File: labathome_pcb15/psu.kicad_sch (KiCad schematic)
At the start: 38 parts, among them J8 POWER, J9 Barrel_Jack_Switch, SW11 PROG 5V POWER, SW5 POWER, U11 AMS1117, U2 IP5306, U24 SRV05, U27 TPS54202DDC

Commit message: labathome15 v0.0.1
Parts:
- added DRAWING1: Polarity, liebler_DRAWINGS:barrel_jack_positive_polarity, symbol Mechanical:Fiducial
- added SW4: BATT POWER, liebler_MECH:Switch_SS12D00, symbol Switch:SW_SPDT
- L1: footprint Inductor_SMD:L_Abracon_ASPI-0630LR -> liebler_PASSIVES:L_0630
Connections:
- net +5V: now also SW4.1 (A); no longer C28.2, C30.2, C31.2, U2.8 (VOUT)
- new net: C28.2, C30.2, C31.2, SW4.2 (B), U2.8 (VOUT)
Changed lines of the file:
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@@
 	)
 	(junction
-		(at 219.71 33.02)
-		(diameter 0)
-		(color 0 0 0 0)
-	)
-	(junction
 		(at 166.37 38.1)
 		(diameter 0)
@@
 	)
 	(junction
+		(at 219.71 33.02)
+		(diameter 0)
+		(color 0 0 0 0)
+	)
+	(junction
 		(at 218.44 35.56)
 		(diameter 0)
@@
 	(wire
 		(pts
+			(xy 246.38 31.75) (xy 226.06 31.75)
+		)
+		(stroke
+			(width 0)
+			(type default)
+		)
+	)
+	(wire
+		(pts
 			(xy 208.28 50.8) (xy 218.44 50.8)
 		)
@@
 	(wire
 		(pts
+			(xy 226.06 31.75) (xy 226.06 33.02)
+		)
+		(stroke
+			(width 0)
+			(type default)
+		)
+	)
+	(wire
+		(pts
 			(xy 80.01 20.32) (xy 80.01 25.4)
 		)
@@
 	(wire
 		(pts
+			(xy 226.06 33.02) (xy 219.71 33.02)
+		)
+		(stroke
+			(width 0)
+			(type default)
+		)
+	)
+	(wire
+		(pts
 			(xy 186.69 33.02) (xy 199.39 33.02)
 		)
@@
 	)
 	(symbol
+		(lib_id "Switch:SW_SPDT")
+		(at 251.46 31.75 0)
+		(unit 1)
+		(exclude_from_sim no)
+		(in_bom yes)
+		(on_board yes)
+		(dnp no)
+		(property "Reference" "SW4"
+			(at 251.46 24.511 0)
+			(effects
+				(font
+					(size 1.27 1.27)
+				)
+			)
+		)
+		(property "Value" "BATT POWER"
+			(at 251.46 36.576 0)
+			(effects
+				(font
+					(size 1.27 1.27)
+				)
+			)
+		)
+		(property "Footprint" "liebler_MECH:Switch_SS12D00"
+			(at 251.46 31.75 0)
+			(effects
+				(font
+					(size 1.27 1.27)
+				)
+				(hide yes)
+			)
+		)
+		(property "Datasheet" "~"
+			(at 251.46 31.75 0)
+			(effects
+				(font
+					(size 1.27 1.27)
+				)
+				(hide yes)
+			)
+		)
+		(property "Description" ""
+			(at 251.46 31.75 0)
+			(effects
+				(font
+					(size 1.27 1.27)
+				)
+				(hide yes)
+			)
+		)
+		(pin "1"
+		)
+		(pin "2"
+		)
+		(pin "3"
+		)
+		(instances
+			(project "labathome_pcb15"
+				(path "/e4d6926a-1a8b-424d-97c4-66b6ad87e4ac/77dfbe0c-d674-478a-bf0e-cfa040fb2e8f"
+					(reference "SW4")
+					(unit 1)
+				)
+			)
+		)
+	)
+	(symbol
 		(lib_id "power:GND")
 		(at 199.39 25.4 180)
@@
 			)
 		)
-		(property "Footprint" "Inductor_SMD:L_Abracon_ASPI-0630LR"
+		(property "Footprint" "liebler_PASSIVES:L_0630"
 			(at 190.5 35.56 0)
 			(effects
@@
 	(symbol
 		(lib_id "power:+5V")
-		(at 219.71 33.02 270)
+		(at 256.54 29.21 270)
+		(mirror x)
 		(unit 1)
 		(exclude_from_sim no)
@@
 		(on_board yes)
 		(dnp no)
-		(fields_autoplaced yes)
 		(property "Reference" "#PWR035"
-			(at 215.9 33.02 0)
+			(at 252.73 29.21 0)
 			(effects
 				(font
@@
 		)
 		(property "Value" "+5V"
-			(at 223.52 33.0199 90)
+			(at 260.35 29.2101 90)
 			(effects
 				(font
@@
 		)
 		(property "Footprint" ""
-			(at 219.71 33.02 0)
+			(at 256.54 29.21 0)
 			(effects
 				(font
@@
 		)
 		(property "Datasheet" ""
-			(at 219.71 33.02 0)
+			(at 256.54 29.21 0)
 			(effects
 				(font
@@
 		)
 		(property "Description" ""
-			(at 219.71 33.02 0)
+			(at 256.54 29.21 0)
 			(effects
 				(font
@@
 					(unit 1)
 				)
+			)
+		)
+	)
+	(symbol
+		(lib_id "Mechanical:Fiducial")
+		(at 97.79 72.39 0)
+		(unit 1)
+		(exclude_from_sim yes)
+		(in_bom no)
+		(on_board yes)
+		(dnp no)
+		(fields_autoplaced yes)
+		(property "Reference" "DRAWING1"
+			(at 100.33 71.1199 0)
+			(effects
+				(font
+					(size 1.27 1.27)
+				)
+				(justify left)
+			)
+		)
+		(property "Value" "Polarity"
+			(at 100.33 73.6599 0)
+			(effects
+				(font
+					(size 1.27 1.27)
+				)
+				(justify left)
+			)
+		)
+		(property "Footprint" "liebler_DRAWINGS:barrel_jack_positive_polarity"
+			(at 97.79 72.39 0)
+			(effects
+				(font
+					(size 1.27 1.27)
+				)
+				(hide yes)
+			)
+		)
+		(property "Datasheet" "~"
+			(at 97.79 72.39 0)
+			(effects
+				(font
+					(size 1.27 1.27)
+				)
+				(hide yes)
+			)
+		)
+		(property "Description" "Fiducial Marker"
+			(at 97.79 72.39 0)
+			(effects
+				(font
+					(size 1.27 1.27)
+				)
+				(hide yes)
+			)
+		)
+		(instances
+			(project ""
+				(path "/e4d6926a-1a8b-424d-97c4-66b6ad87e4ac/77dfbe0c-d674-478a-bf0e-cfa040fb2e8f"
+					(reference "DRAWING1")
+					(unit 1)
+				)

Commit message: labathome_pcb15
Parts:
- added R47: 1R, Resistor_SMD:R_0603_1608Metric, symbol Device:R
- added R48: 3k3, Resistor_SMD:R_0402_1005Metric, symbol Device:R
- C41, C42, C43, C44: footprint Capacitor_SMD:C_0603_1608Metric -> Capacitor_SMD:C_0402_1005Metric
- C79: value u1 -> u1/35V
- C80: value 10u -> 10u/35V
- C81: value u1 -> u1/16V
- R3: value 2R2 -> 1R
- R4: footprint Resistor_SMD:R_0603_1608Metric -> Resistor_SMD:R_0402_1005Metric
- R60: value 13k3 -> 10k
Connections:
- net +5P: now also R47.1; no longer R3.1
- net GND: now also R48.1; no longer R60.1
- new net: R48.2, R60.1
- new net: R3.1, R47.2
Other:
- moved on the sheet: C1

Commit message: labathome_pcb5 ready for review, 2nd
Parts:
- removed DRAWING1: Polarity, liebler_DRAWINGS:barrel_jack_positive_polarity, symbol Mechanical:Fiducial
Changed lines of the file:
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@@
-	)
-	(symbol
-		(lib_id "Mechanical:Fiducial")
-		(at 97.79 72.39 0)
-		(unit 1)
-		(exclude_from_sim yes)
-		(in_bom no)
-		(on_board yes)
-		(dnp no)
-		(fields_autoplaced yes)
-		(property "Reference" "DRAWING1"
-			(at 100.33 71.1199 0)
-			(effects
-				(font
-					(size 1.27 1.27)
-				)
-				(justify left)
-			)
-		)
-		(property "Value" "Polarity"
-			(at 100.33 73.6599 0)
-			(effects
-				(font
-					(size 1.27 1.27)
-				)
-				(justify left)
-			)
-		)
-		(property "Footprint" "liebler_DRAWINGS:barrel_jack_positive_polarity"
-			(at 97.79 72.39 0)
-			(effects
-				(font
-					(size 1.27 1.27)
-				)
-				(hide yes)
-			)
-		)
-		(property "Datasheet" "~"
-			(at 97.79 72.39 0)
-			(effects
-				(font
-					(size 1.27 1.27)
-				)
-				(hide yes)
-			)
-		)
-		(property "Description" "Fiducial Marker"
-			(at 97.79 72.39 0)
-			(effects
-				(font
-					(size 1.27 1.27)
-				)
-				(hide yes)
-			)
-		)
-		(instances
-			(project ""
-				(path "/e4d6926a-1a8b-424d-97c4-66b6ad87e4ac/77dfbe0c-d674-478a-bf0e-cfa040fb2e8f"
-					(reference "DRAWING1")
-					(unit 1)
-				)
-			)
-		)
 	)
 	(symbol

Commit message: Further improventents in PCB layout
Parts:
- J8: symbol Connector:USB_C_Receptacle_USB2.0 -> Connector:USB_C_Receptacle_USB2.0_16P
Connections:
- no-connect marks 4 -> 5
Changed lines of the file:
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@@
 	)
 	(junction
+		(at 213.36 35.56)
+		(diameter 0)
+		(color 0 0 0 0)
+	)
+	(junction
 		(at 218.44 35.56)
 		(diameter 0)
@@
 		(at 40.64 52.07)
 	)
+	(no_connect
+		(at 256.54 34.29)
+	)
 	(wire
 		(pts
@@
 	(wire
 		(pts
-			(xy 208.28 35.56) (xy 218.44 35.56)
+			(xy 208.28 35.56) (xy 213.36 35.56)
 		)
 		(stroke
@@
 		)
 	)
+	(wire
+		(pts
+			(xy 213.36 35.56) (xy 218.44 35.56)
+		)
+		(stroke
+			(width 0)
+			(type default)
+		)
+	)
 	(polyline
 		(pts
@@
 			)
 		)
-		(property "Description" ""
+		(property "Description" "Power symbol creates a global label with name \"+5VP\""
 			(at 121.92 33.02 0)
 			(effects
@@
 			)
 		)
-		(property "Description" ""
+		(property "Description" "Power symbol creates a global label with name \"GND\" , ground"
 			(at 209.55 25.4 0)
 			(effects
@@
 			)
 		)
-		(property "Description" ""
+		(property "Description" "Power symbol creates a global label with name \"+5P\""
 			(at 100.33 100.33 0)
 			(effects
@@
 			)
 		)
-		(property "Description" ""
+		(property "Description" "Power symbol creates a global label with name \"+5V\""
 			(at 110.49 102.87 0)
 			(effects
@@
 			)
 		)
-		(property "Description" ""
+		(property "Description" "Power symbol creates a global label with name \"+24V\""
 			(at 82.55 80.01 0)
 			(effects
@@
 			)
 		)
-		(property "Description" ""
+		(property "Description" "Switch, single pole double throw"
 			(at 251.46 31.75 0)
 			(effects
@@
 			)
 		)
-		(property "Description" ""
+		(property "Description" "Power symbol creates a global label with name \"GND\" , ground"
 			(at 199.39 25.4 0)
 			(effects
@@
 			)
 		)
-		(property "Description" ""
+		(property "Description" "Power symbol creates a global label with name \"+5V\""
 			(at 17.78 73.66 0)
 			(effects
@@
 			)
 		)
-		(property "Description" ""
+		(property "Description" "Power symbol creates a global label with name \"+24V\""
 			(at 48.26 21.59 0)
 			(effects
@@
 			)
 		)
-		(property "Description" ""
+		(property "Description" "Power symbol creates a global label with name \"GND\" , ground"
 			(at 171.45 52.07 0)
 			(effects
@@
 			)
 		)
-		(property "Description" ""
+		(property "Description" "Power symbol creates a global label with name \"GND\" , ground"
 			(at 43.18 124.46 0)
 			(effects
@@
 			)
 		)
-		(property "Description" ""
+		(property "Description" "Special symbol for telling ERC where power comes from"
 			(at 110.49 102.87 0)
 			(effects
@@
 			)
 		)
-		(property "Description" ""
+		(property "Description" "1A Low Dropout regulator, positive, 3.3V fixed output, SOT-223"
 			(at 38.1 73.66 0)
 			(effects
@@
 			)
 		)
-		(property "Description" ""
+		(property "Description" "Power symbol creates a global label with name \"GND\" , ground"
 			(at 179.07 44.45 0)
 			(effects
@@
 			)
 		)
-		(property "Description" ""
+		(property "Description" "Power symbol creates a global label with name \"+5V\""
 			(at 256.54 29.21 0)
 			(effects
@@
 			)
 		)
-		(property "Description" ""
+		(property "Description" "Special symbol for telling ERC where power comes from"
 			(at 40.64 21.59 0)
 			(effects
@@
 			)
 		)
-		(property "Description" ""
+		(property "Description" "Special symbol for telling ERC where power comes from"
 			(at 91.44 105.41 0)
 			(effects
@@
 			)
 		)
-		(property "Description" ""
+		(property "Description" "Switch, single pole double throw"
 			(at 105.41 102.87 0)
 			(effects
@@
 			)
 		)
-		(property "Description" ""
+		(property "Description" "Power symbol creates a global label with name \"GND\" , ground"
 			(at 55.88 81.28 0)
 			(effects
@@
 			)
 		)
-		(property "Description" ""
+		(property "Description" "Power symbol creates a global label with name \"GND\" , ground"
 			(at 194.31 50.8 0)
 			(effects
@@
 			)
 		)
-		(property "Description" ""
+		(property "Description" "Power symbol creates a global label with name \"GND\" , ground"
 			(at 80.01 50.8 0)
 			(effects
@@
 	)
 	(symbol
-		(lib_id "Connector:USB_C_Receptacle_USB2.0")
+		(lib_id "Connector:USB_C_Receptacle_USB2.0_16P")
 		(at 25.4 36.83 0)
 		(unit 1)
@@
 			)
 		)
-		(property "Description" ""
+		(property "Description" "USB 2.0-only 16P Type-C Receptacle connector"
 			(at 25.4 36.83 0)
 			(effects
@@
 			)
 		)
-		(property "Description" ""
+		(property "Description" "Power symbol creates a global label with name \"GND\" , ground"
 			(at 219.71 25.4 0)
 			(effects
@@
 			)
 		)
-		(property "Description" ""
+		(property "Description" "Power symbol creates a global label with name \"GND\" , ground"
 			(at 132.08 57.15 0)
 			(effects
@@
 			)
 		)
-		(property "Description" ""
+		(property "Description" "Power symbol creates a global label with name \"GND\" , ground"
 			(at 82.55 74.93 0)
 			(effects
@@
 			)
 		)
-		(property "Description" ""
+		(property "Description" "Power symbol creates a global label with name \"+3V8\""
 			(at 218.44 35.56 0)
 			(effects
@@
 			)
 		)
-		(property "Description" ""
+		(property "Description" "Power symbol creates a global label with name \"GND\" , ground"
 			(at 25.4 59.69 0)
 			(effects
@@
 			)
 		)
-		(property "Description" ""
+		(property "Description" "Power symbol creates a global label with name \"+3V3\""
 			(at 55.88 73.66 0)
 			(effects
@@
 			)
 		)
-		(property "Description" ""
+		(property "Description" "Power symbol creates a global label with name \"+24V\""
 			(at 25.4 106.68 0)
 			(effects
@@
 	)
 	(symbol
+		(lib_id "power:PWR_FLAG")
+		(at 213.36 35.56 180)
+		(unit 1)
+		(exclude_from_sim no)
+		(in_bom yes)
+		(on_board yes)
+		(dnp no)
+		(fields_autoplaced yes)
+		(property "Reference" "#FLG09"
+			(at 213.36 37.465 0)
+			(effects
+				(font
+					(size 1.27 1.27)
+				)
+				(hide yes)
+			)
+		)
+		(property "Value" "PWR_FLAG"
+			(at 213.36 40.64 0)
+			(effects
+				(font
+					(size 1.27 1.27)
+				)
+			)
+		)
+		(property "Footprint" ""
+			(at 213.36 35.56 0)
+			(effects
+				(font
+					(size 1.27 1.27)
+				)
+				(hide yes)
+			)
+		)
+		(property "Datasheet" "~"
+			(at 213.36 35.56 0)
+			(effects
+				(font
+					(size 1.27 1.27)
+				)
+				(hide yes)
+			)
+		)
+		(property "Description" "Special symbol for telling ERC where power comes from"
+			(at 213.36 35.56 0)
+			(effects
+				(font
+					(size 1.27 1.27)
+				)
+				(hide yes)
+			)
+		)
+		(pin "1"
+		)
+		(instances
+			(project ""
+				(path "/e4d6926a-1a8b-424d-97c4-66b6ad87e4ac/77dfbe0c-d674-478a-bf0e-cfa040fb2e8f"
+					(reference "#FLG09")
+					(unit 1)
+				)
+			)
+		)
+	)
+	(symbol
 		(lib_id "Device:Battery_Cell")
 		(at 218.44 44.45 0)
@@
 			)
 		)
-		(property "Description" ""
+		(property "Description" "Single-cell battery"
 			(at 218.44 44.45 0)
 			(effects

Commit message: lbathome 15.1
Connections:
- net USBPD_CC1: now also U24.3 (IO2); no longer U24.1 (IO1)
- net USBPD_D-: now also U24.1 (IO1); no longer U24.3 (IO2)
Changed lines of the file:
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@@
 	(global_label "USBPD_D-"
 		(shape input)
-		(at 92.71 40.64 0)
+		(at 92.71 35.56 0)
 		(fields_autoplaced yes)
 		(effects
@@
 		)
 		(property "Intersheetrefs" "${INTERSHEET_REFS}"
-			(at 105.8552 40.64 0)
+			(at 105.8552 35.56 0)
 			(effects
 				(font
@@
 	(global_label "USBPD_CC1"
 		(shape input)
-		(at 92.71 35.56 0)
+		(at 92.71 40.64 0)
 		(fields_autoplaced yes)
 		(effects
@@
 		)
 		(property "Intersheetrefs" "${INTERSHEET_REFS}"
-			(at 106.7623 35.56 0)
+			(at 106.7623 40.64 0)
 			(effects
 				(font

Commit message: Updates in PCB, arduino test firmware
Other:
- company: (none) -> Klaus Liebler
- title: (none) -> lab@home
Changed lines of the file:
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@@
 	(generator_version "8.0")
 	(paper "A4")
+	(title_block
+		(title "lab@home")
+		(date "2024-08-19")
+		(rev "15.1")
+		(company "Klaus Liebler")
+	)
 	(junction
 		(at 157.48 45.72)

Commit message: Various last minute
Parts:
- C81: footprint Capacitor_SMD:C_0402_1005Metric -> Capacitor_SMD:C_0603_1608Metric
- R4, R48, R59, R60: footprint Resistor_SMD:R_0402_1005Metric -> Resistor_SMD:R_0201_0603Metric
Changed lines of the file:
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@@
 			)
 		)
-		(property "Footprint" "Resistor_SMD:R_0402_1005Metric"
+		(property "Footprint" "Resistor_SMD:R_0201_0603Metric"
 			(at 88.138 124.46 90)
 			(effects
@@
 			)
 		)
-		(property "Footprint" "Resistor_SMD:R_0402_1005Metric"
+		(property "Footprint" "Resistor_SMD:R_0201_0603Metric"
 			(at 88.138 116.84 90)
 			(effects
@@
 			)
 		)
-		(property "Footprint" "Resistor_SMD:R_0402_1005Metric"
+		(property "Footprint" "Resistor_SMD:R_0201_0603Metric"
 			(at 84.582 109.22 90)
 			(effects
@@
 			)
 		)
-		(property "Footprint" "Capacitor_SMD:C_0402_1005Metric"
+		(property "Footprint" "Capacitor_SMD:C_0603_1608Metric"
 			(at 54.9148 100.33 0)
 			(effects
@@
 			)
 		)
-		(property "Footprint" "Resistor_SMD:R_0402_1005Metric"
+		(property "Footprint" "Resistor_SMD:R_0201_0603Metric"
 			(at 185.42 50.292 90)
 			(effects

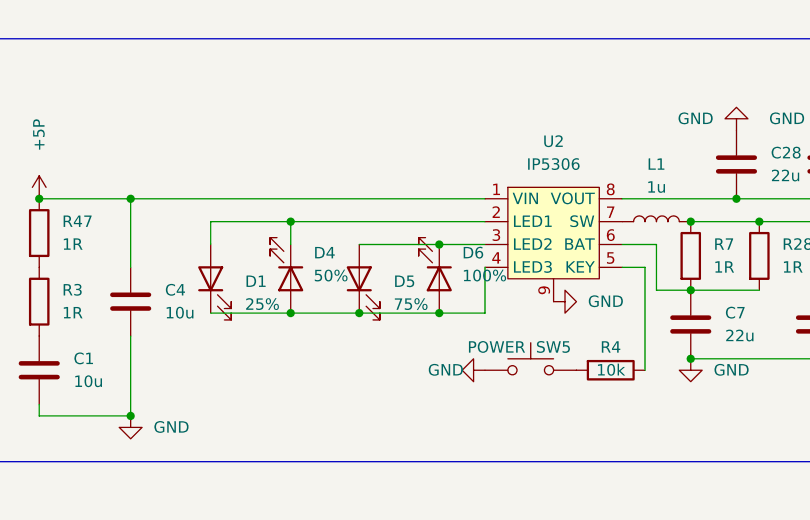
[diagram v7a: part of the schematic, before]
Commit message: PCB update IP5306 I2C
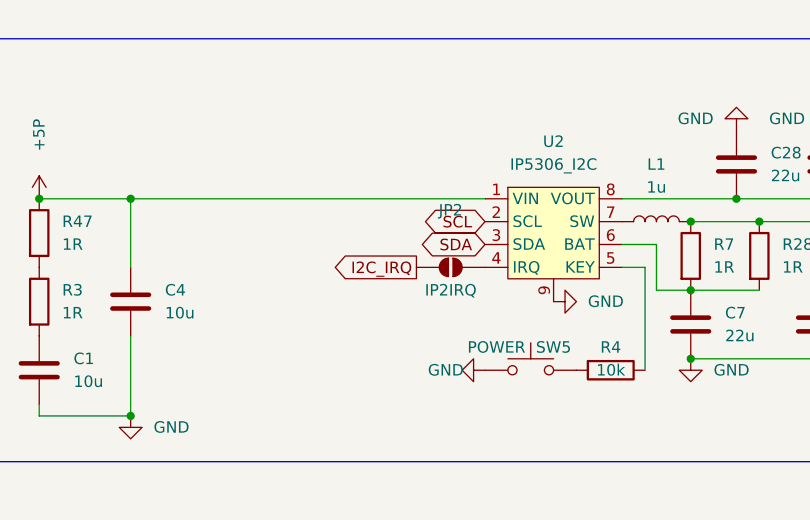
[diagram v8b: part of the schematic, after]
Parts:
- removed D1: 25%, LED_SMD:LED_0805_2012Metric_Pad1.15x1.40mm_HandSolder, symbol Device:LED
- removed D4: 50%, LED_SMD:LED_0805_2012Metric_Pad1.15x1.40mm_HandSolder, symbol Device:LED
- removed D5: 75%, LED_SMD:LED_0805_2012Metric_Pad1.15x1.40mm_HandSolder, symbol Device:LED
- removed D6: 100%, LED_SMD:LED_0805_2012Metric_Pad1.15x1.40mm_HandSolder, symbol Device:LED
- removed U2: IP5306, Package_SO:HSOP-8-1EP_3.9x4.9mm_P1.27mm_EP2.3x2.3mm_ThermalVias, symbol liebler_SEMICONDUCTORS:IP5306
- added JP2: IP2IRQ, Jumper:SolderJumper-2_P1.3mm_Open_RoundedPad1.0x1.5mm, symbol Jumper:SolderJumper_2_Open
- added U2: IP5306_I2C, Package_SO:HSOP-8-1EP_3.9x4.9mm_P1.27mm_EP2.3x2.3mm_ThermalVias, symbol liebler_SEMICONDUCTORS:IP5306_I2C
- SW5: footprint liebler_MECH:SW_SPST_TL3342_smaller_handsolder -> liebler_MECH:SW_Push_1P1T_NO_6x6mm_H6.5mm_Reverse
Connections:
- net +5P: now also U2.1 (VIN)
- net GND: now also U2.9
- net at C28.2, C30.2, C31.2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: now also U2.8 (VOUT)
- net at L1.1: now also U2.7 (SW)
- net at C7.1, R28.2, R7.2: now also U2.6 (BAT)
- net at R4.1: now also U2.5 (KEY)
- new net: JP2.2 (B), U2.4 (IRQ)
- new net I2C_IRQ: JP2.1 (A)
- new net SCL: U2.2 (SCL)
- new net SDA: U2.3 (SDA)
